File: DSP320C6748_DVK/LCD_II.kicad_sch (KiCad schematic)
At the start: 1 part, among them IC9 THS8135PHP

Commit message: LCD Schematic Completed
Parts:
- added C109, C110, C111, C112, C113, C114, C115: 0.1uF/16V/X7R, symbol Device:C_Small
- added IC12: SN74AVC16T245DGG, SOP50P810X120-48N, symbol SN74AVC16T245DGG:SN74AVC16T245DGG
- added R123, R124, R125, R130, R131: 4.7K,5%,1/16W, symbol Device:R_Small
- added R126: 3.4K,1%,1/16W, symbol Device:R_Small
- added R127, R128, R129: 75R,5%,1/16W, symbol Device:R_Small
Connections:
- net LCD_1V8_D_4: now reaches IC9.1 (BCB9)
- net LCD_1V8_D_4: now also IC9.6 (BCB4), IC12.41 (1A5)
- net LCD_1V8_D_0: now reaches IC9.10 (BCB0)
- net LCD_1V8_D_0: now also IC9.5 (BCB5), IC12.47 (1A1)
- net +1V8D: now reaches IC9.12 (DVDD)
- net +1V8D: now also C109.1, C114.2, C115.2, IC12.31 (VCCA_1), IC12.42 (VCCA_2), R123.1, R124.1, R125.1
- net LCD_1V8_D_11: now reaches IC9.13 (RCR0)
- net LCD_1V8_D_11: now also IC9.18 (RCR5), IC12.32 (2A4)
- net LCD_1V8_D_12: now reaches IC9.14 (RCR1)
- net LCD_1V8_D_12: now also IC9.19 (RCR6), IC12.30 (2A5)
- net LCD_1V8_D_13: now reaches IC9.15 (RCR2)
- net LCD_1V8_D_13: now also IC9.20 (RCR7), IC12.29 (2A6)
- net LCD_1V8_D_14: now reaches IC9.16 (RCR3)
- net LCD_1V8_D_14: now also IC9.21 (RCR8), IC12.27 (2A7)
- net LCD_1V8_D_15: now reaches IC9.17 (RCR4)
- net LCD_1V8_D_15: now also IC9.22 (RCR9), IC12.26 (2A8)
- net LCD_1V8_D_3: now reaches IC9.2 (BCB8)
- net LCD_1V8_D_3: now also IC9.7 (BCB3), IC12.43 (1A4)
- net LCD_AC_ENB_~{CS}_1V8: now reaches IC9.23 (~{BLANK})
- net LCD_AC_ENB_~{CS}_1V8: now also R123.2
- net ~{SYNC}: now reaches IC9.24 (~{SYNC})
- net ~{SYNC}: now also R124.2
- net SYNC_T: now reaches IC9.25 (SYNC_T)
- net SYNC_T: now also R125.2
- net LCD_PCLK_1V8: now reaches IC9.26 (CLK)
- net LCD_1V8_D_10: now reaches IC9.27 (GY9)
- net LCD_1V8_D_10: now also IC9.33 (GY3), IC12.33 (2A3)
- net LCD_1V8_D_9: now reaches IC9.28 (GY8)
- net LCD_1V8_D_9: now also IC9.34 (GY2), IC12.35 (2A2)
- net LCD_1V8_D_8: now reaches IC9.29 (GY7)
- net LCD_1V8_D_8: now also IC9.35 (GY1), IC12.36 (2A1)
- net LCD_1V8_D_2: now reaches IC9.3 (BCB7)
- net LCD_1V8_D_2: now also IC9.8 (BCB2), IC12.44 (1A3)
- net LCD_1V8_D_7: now reaches IC9.30 (GY6)
- net LCD_1V8_D_7: now also IC9.36 (GY0), IC12.37 (1A8)
- net LCD_1V8_D_6: now reaches IC9.31 (GY5)
- net LCD_1V8_D_6: now also IC12.38 (1A7)
- net LCD_1V8_D_5: now reaches IC9.32 (GY4)
- net LCD_1V8_D_5: now also IC12.40 (1A6)
- net at IC9.37 (VREF): now also C111.1
- net FSADJ: now reaches IC9.38 (FSADJ)
- net FSADJ: now also R126.1
- net COMP: now reaches IC9.39 (COMP)
- net COMP: now also C110.2
- net LCD_1V8_D_1: now reaches IC9.4 (BCB6)
- net LCD_1V8_D_1: now also IC9.9 (BCB1), IC12.46 (1A2)
- net +3V3ADAC: now reaches IC9.40 (AVDD_1)
- net +3V3ADAC: now also IC9.44 (AVDD_2), C110.1
- net AGY: now reaches IC9.41 (AGY)
- net AGY: now also R127.1
- net GND: now reaches IC9.42 (AVSS_1)
- net GND: now also IC9.46 (AVSS_2), IC9.49 (EP), C109.2, C111.2, C112.1, C113.1, C114.1, C115.1, IC12.1 (1DIR), IC12.10 (GND_2), IC12.15 (GND_3), IC12.21 (GND_4), IC12.24 (2DIR), IC12.25 (2~{OE}), IC12.28 (GND_5), IC12.34 (GND_6), IC12.39 (GND_7), IC12.4 (GND_1), IC12.45 (GND_8), IC12.48 (1~{OE}), R126.2, R127.2, R128.2, R129.2, R130.2, R131.2
- net ARPR: now reaches IC9.43 (ARPR)
- net ARPR: now also R128.1
- net ABPB: now reaches IC9.45 (ABPB)
- net ABPB: now also R129.1
- net M1: now reaches IC9.47 (M1)
- net M1: now also R131.1
- net M2: now reaches IC9.48 (M2)
- net M2: now also R130.1
- new net +3V3D: C112.2, C113.2, IC12.18 (VCCB_2), IC12.7 (VCCB_1)
- new net VPIF_DOUT_{0}: IC12.2 (1B1)
- new net VPIF_DOUT_{10}: IC12.16 (2B3)
- new net VPIF_DOUT_{11}: IC12.17 (2B4)
- new net VPIF_DOUT_{12}: IC12.19 (2B5)
- new net VPIF_DOUT_{13}: IC12.20 (2B6)
- new net VPIF_DOUT_{14}: IC12.22 (2B7)
- new net VPIF_DOUT_{15}: IC12.23 (2B8)
- new net VPIF_DOUT_{1}: IC12.3 (1B2)
- new net VPIF_DOUT_{2}: IC12.5 (1B3)
- new net VPIF_DOUT_{3}: IC12.6 (1B4)
- new net VPIF_DOUT_{4}: IC12.8 (1B5)
- new net VPIF_DOUT_{5}: IC12.9 (1B6)
- new net VPIF_DOUT_{6}: IC12.11 (1B7)
- new net VPIF_DOUT_{7}: IC12.12 (1B8)
- new net VPIF_DOUT_{8}: IC12.13 (2B1)
- new net VPIF_DOUT_{9}: IC12.14 (2B2)
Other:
- moved on the sheet: IC9

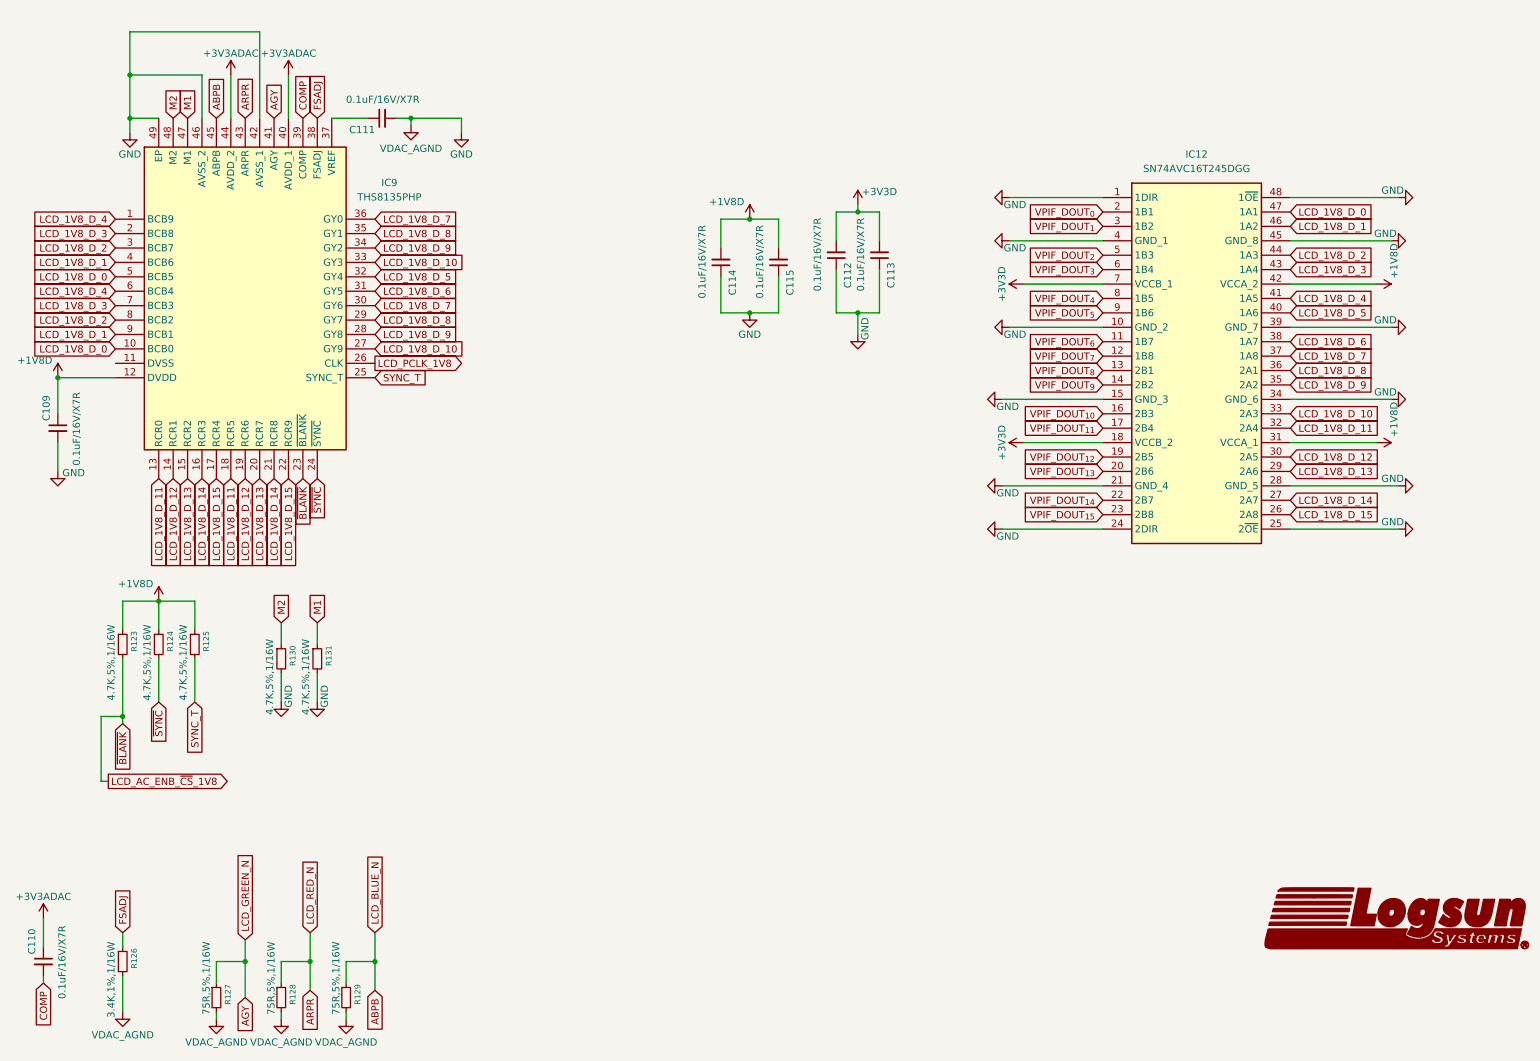
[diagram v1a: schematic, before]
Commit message: Connectors and mislleneous components added
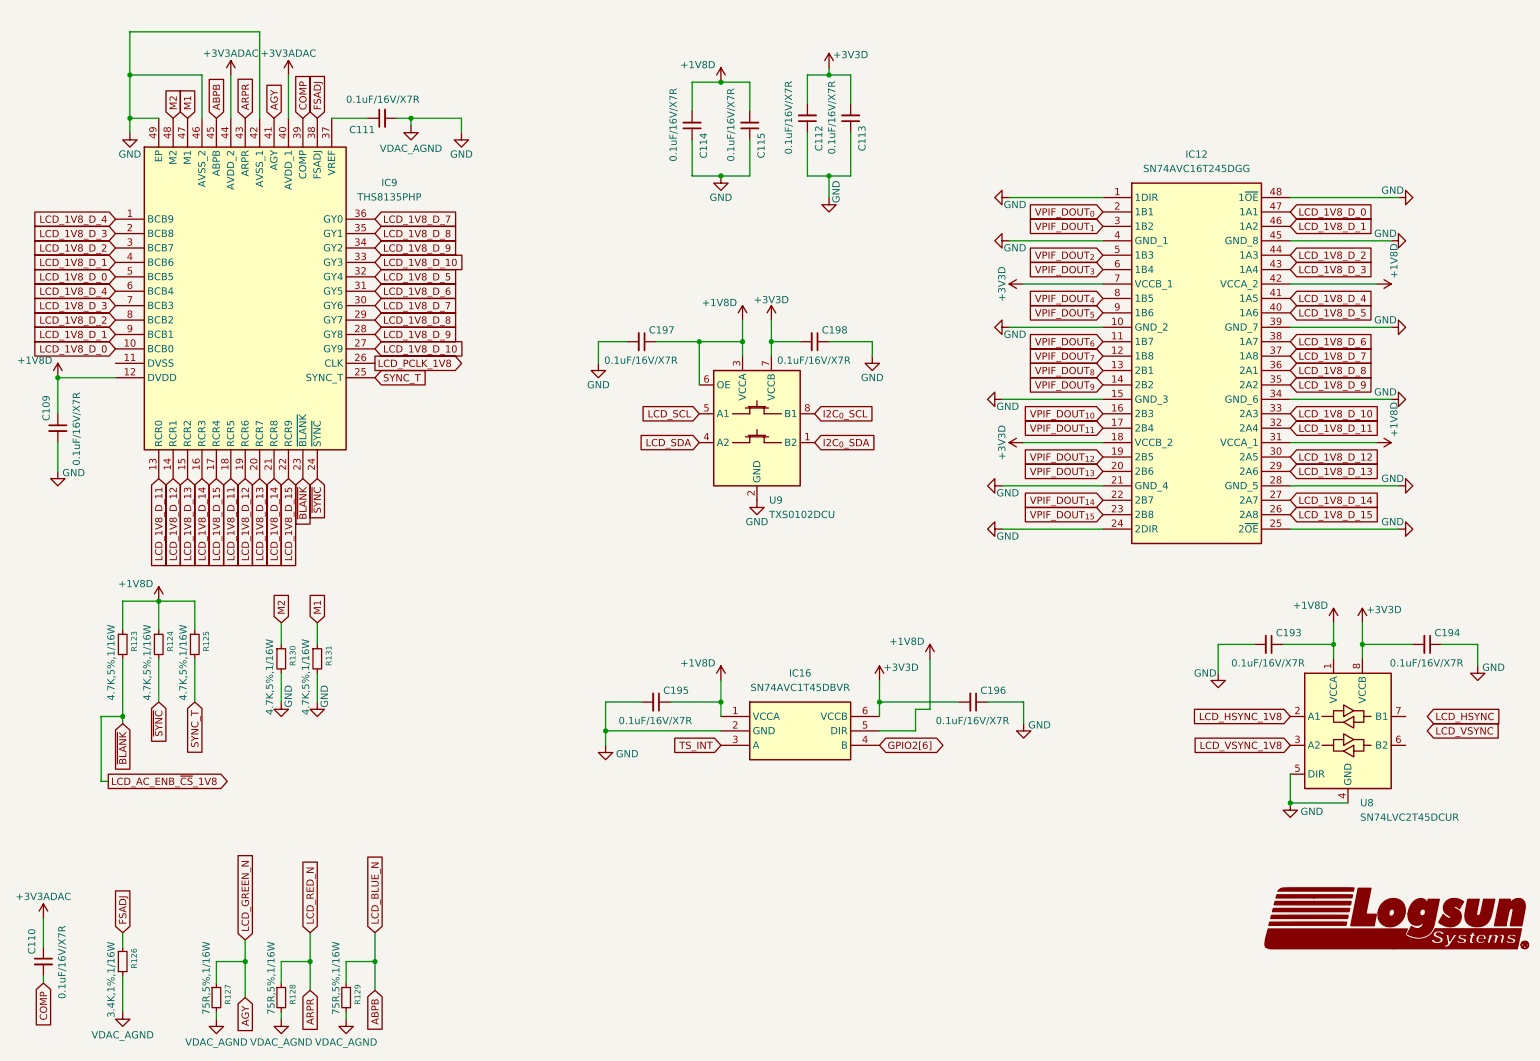
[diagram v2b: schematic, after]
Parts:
- added C193, C194, C195, C196, C197, C198: 0.1uF/16V/X7R, symbol Device:C_Small
- added IC16: SN74AVC1T45DBVR, SOT95P280X145-6N, symbol SN74AVC1T45DBVR:SN74AVC1T45DBVR
- added U8: SN74LVC2T45DCUR, Package_SO:VSSOP-8_2.3x2mm_P0.5mm, symbol Logic_LevelTranslator:SN74LVC2T45DCUR
- added U9: TXS0102DCU, Package_SO:VSSOP-8_2.3x2mm_P0.5mm, symbol Logic_LevelTranslator:TXS0102DCU
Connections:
- net +1V8D: now also C193.1, C195.1, C197.1, IC16.1 (VCCA), IC16.5 (DIR), U8.1 (VCCA), U9.3 (VCCA), U9.6 (OE)
- net +3V3D: now also C194.2, C196.2, C198.2, IC16.6 (VCCB), U8.8 (VCCB), U9.7 (VCCB)
- net GND: now also C193.2, C194.1, C195.2, C196.1, C197.2, C198.1, IC16.2 (GND), U8.4 (GND), U8.5 (DIR), U9.2 (GND)
- new net GPIO2[6]: IC16.4 (B)
- new net I2C_{0}_SCL: U9.8 (B1)
- new net I2C_{0}_SDA: U9.1 (B2)
- new net LCD_HSYNC_1V8: U8.2 (A1)
- new net LCD_SCL: U9.5 (A1)
- new net LCD_SDA: U9.4 (A2)
- new net LCD_VSYNC_1V8: U8.3 (A2)
- new net TS_INT: IC16.3 (A)
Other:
- moved on the sheet: C112, C113, C114, C115

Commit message: Whole Schematic Reannotation Done
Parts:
- renumbered C110 to C109, C109 to C110, C197 to C112, C195 to C113, C112 to C116, C198 to C117, C113 to C118, C196 to C119, C193 to C120, C194 to C121, IC9 to IC11, IC16 to IC12, IC12 to IC13, R130 to R100, R128 to R101, R131 to R102, R129 to R103, R123 to R95, R126 to R96, R124 to R97, R125 to R98, R127 to R99, U9 to U6, U8 to U7

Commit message: Schematic Corrections-II Done
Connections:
- net GND: now also IC11.11 (DVSS)
- net LCD_HSYNC: now also U7.7 (B1)
- net LCD_VSYNC: now also U7.6 (B2)
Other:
- moved on the sheet: C114, C115, C116, C118

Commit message: DC jack Replaced With Type-C, ADC and RTC section added
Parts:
- renumbered C109 to C111, C110 to C112, C111 to C113, C112 to C114, C113 to C115, C117 to C116, C119 to C117, C120 to C118, C114 to C119, C115 to C120, C116 to C122, C118 to C123, R99 to R100, R100 to R101, R101 to R102, R102 to R103, R103 to R104, R95 to R96, R96 to R97, R97 to R98, R98 to R99

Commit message: Scheamtic Re-annotation done, Some footprints assigned
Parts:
- C114: renamed from C111; footprint (none) -> Capacitor_SMD:C_0603_1608Metric_Pad1.08x0.95mm_HandSolder
- C115: renamed from C112; footprint (none) -> Capacitor_SMD:C_0603_1608Metric_Pad1.08x0.95mm_HandSolder
- C116: renamed from C113; footprint (none) -> Capacitor_SMD:C_0603_1608Metric_Pad1.08x0.95mm_HandSolder
- C117: renamed from C114; footprint (none) -> Capacitor_SMD:C_0603_1608Metric_Pad1.08x0.95mm_HandSolder
- C118: renamed from C115; footprint (none) -> Capacitor_SMD:C_0603_1608Metric_Pad1.08x0.95mm_HandSolder
- C119: renamed from C116; footprint (none) -> Capacitor_SMD:C_0603_1608Metric_Pad1.08x0.95mm_HandSolder
- C120: renamed from C117; footprint (none) -> Capacitor_SMD:C_0603_1608Metric_Pad1.08x0.95mm_HandSolder
- C121: renamed from C118; footprint (none) -> Capacitor_SMD:C_0603_1608Metric_Pad1.08x0.95mm_HandSolder
- C122: renamed from C119; footprint (none) -> Capacitor_SMD:C_0603_1608Metric_Pad1.08x0.95mm_HandSolder
- C123: renamed from C120; footprint (none) -> Capacitor_SMD:C_0603_1608Metric_Pad1.08x0.95mm_HandSolder
- C124: renamed from C121; footprint (none) -> Capacitor_SMD:C_0603_1608Metric_Pad1.08x0.95mm_HandSolder
- C125: renamed from C122; footprint (none) -> Capacitor_SMD:C_0603_1608Metric_Pad1.08x0.95mm_HandSolder
- C126: renamed from C123; footprint (none) -> Capacitor_SMD:C_0603_1608Metric_Pad1.08x0.95mm_HandSolder
- R100: renamed from R98; footprint (none) -> Resistor_SMD:R_0603_1608Metric_Pad0.98x0.95mm_HandSolder
- R101: renamed from R99; footprint (none) -> Resistor_SMD:R_0603_1608Metric_Pad0.98x0.95mm_HandSolder
- R102: renamed from R100; footprint (none) -> Resistor_SMD:R_0603_1608Metric_Pad0.98x0.95mm_HandSolder
- R103: renamed from R101; footprint (none) -> Resistor_SMD:R_0603_1608Metric_Pad0.98x0.95mm_HandSolder
- R104: renamed from R102; footprint (none) -> Resistor_SMD:R_0603_1608Metric_Pad0.98x0.95mm_HandSolder
- R105: renamed from R103; footprint (none) -> Resistor_SMD:R_0603_1608Metric_Pad0.98x0.95mm_HandSolder
- R106: renamed from R104; footprint (none) -> Resistor_SMD:R_0603_1608Metric_Pad0.98x0.95mm_HandSolder
- R98: renamed from R96; footprint (none) -> Resistor_SMD:R_0603_1608Metric_Pad0.98x0.95mm_HandSolder
- R99: renamed from R97; footprint (none) -> Resistor_SMD:R_0603_1608Metric_Pad0.98x0.95mm_HandSolder
